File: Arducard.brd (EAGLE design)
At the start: 90 x 50 mm, 19 parts, among them U1 ATMEGA328P, U2 MPR121V2, U3 TPS61097-33DBVR, Y1 8MHZ

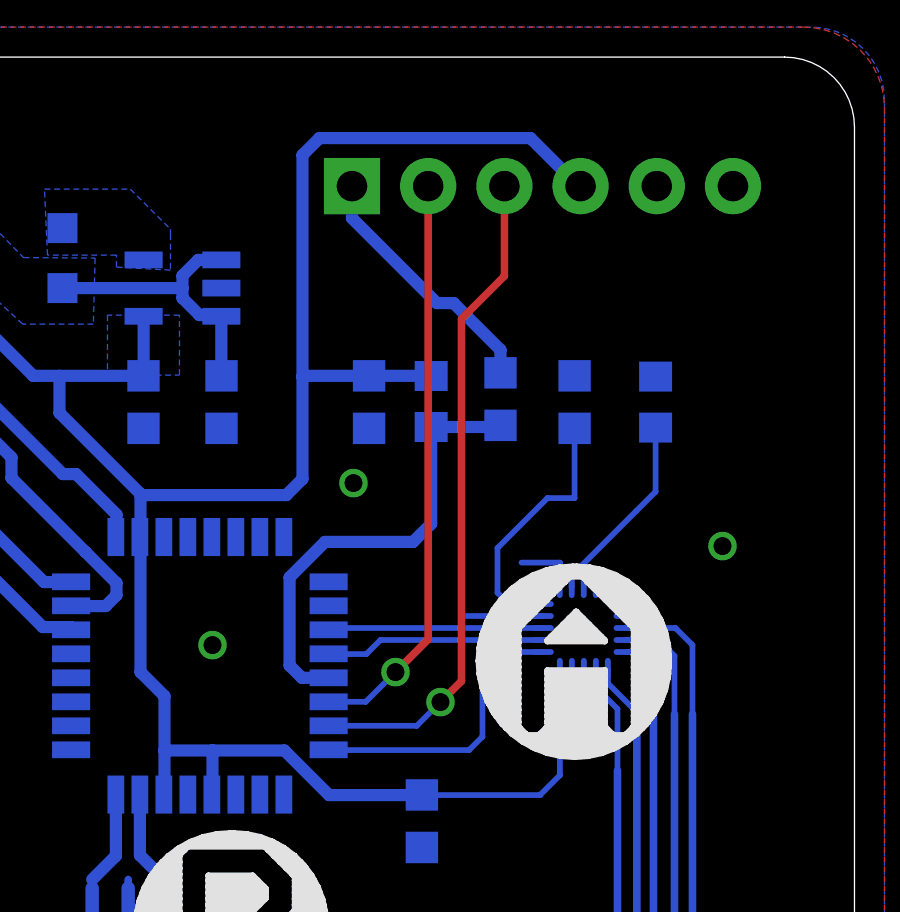
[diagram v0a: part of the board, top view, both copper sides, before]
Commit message: Fixed minor errors
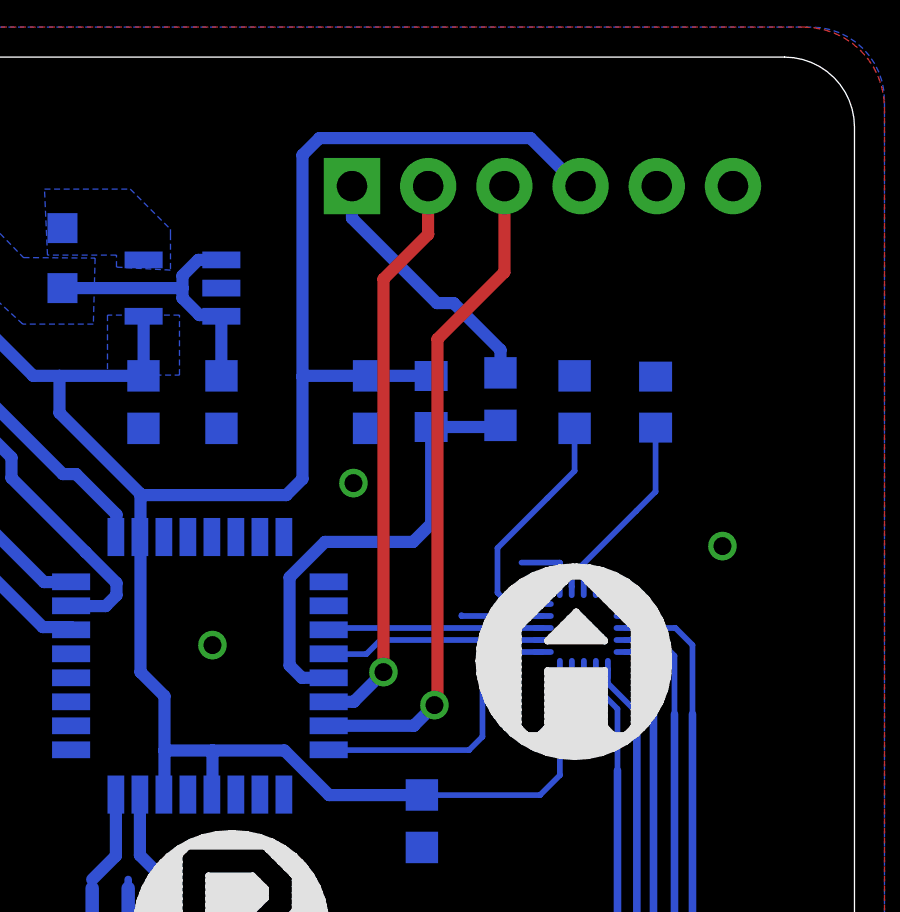
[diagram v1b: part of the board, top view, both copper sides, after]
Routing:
- net N$6: track 8.73 -> 8.20 mm
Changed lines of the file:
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@@
 </class>
 </classes>
-<designrules name="oshPark *">
+<designrules name="oshPark">
 <description language="de">&lt;b&gt;EAGLE Design Rules&lt;/b&gt;
 &lt;p&gt;
@@
 <param name="mlMinCreamFrame" value="0mil"/>
 <param name="mlMaxCreamFrame" value="0mil"/>
-<param name="mlViaStopLimit" value="25mil"/>
+<param name="mlViaStopLimit" value="0mil"/>
 <param name="srRoundness" value="0"/>
 <param name="srMinRoundness" value="0mil"/>
@@
 <wire x1="78.1" y1="32.14801875" x2="78.1" y2="33.63566875" width="0.1905" layer="16"/>
 <wire x1="78.1" y1="33.63566875" x2="79.76433125" y2="35.3" width="0.1905" layer="16"/>
-<wire x1="79.76433125" y1="35.3" x2="80.67" y2="35.3" width="0.1905" layer="16"/>
-<wire x1="80.67" y1="35.3" x2="80.67" y2="37.625" width="0.1905" layer="16"/>
+<wire x1="79.76433125" y1="35.3" x2="80.67" y2="36.20566875" width="0.1905" layer="16"/>
+<wire x1="80.67" y1="36.20566875" x2="80.67" y2="37.625" width="0.1905" layer="16"/>
 </signal>
 <signal name="N$10">
@@
 <contactref element="JP1" pad="P$2"/>
 <contactref element="U1" pad="30"/>
-<wire x1="72.4726" y1="28.51" x2="73.71" y2="28.51" width="0.1905" layer="16"/>
-<wire x1="73.71" y1="28.51" x2="74.7" y2="29.5" width="0.1905" layer="16"/>
-<via x="74.7" y="29.5" extent="1-16" drill="0.6"/>
-<wire x1="74.7" y1="29.5" x2="75.79" y2="30.59" width="0.254" layer="1"/>
-<wire x1="75.79" y1="30.59" x2="75.79" y2="45.7" width="0.254" layer="1"/>
+<wire x1="72.4726" y1="28.51" x2="73.31" y2="28.51" width="0.4064" layer="16"/>
+<wire x1="73.31" y1="28.51" x2="74.3" y2="29.5" width="0.4064" layer="16"/>
+<via x="74.3" y="29.5" extent="1-16" drill="0.6"/>
+<wire x1="74.3" y1="29.5" x2="74.3" y2="42.6" width="0.4064" layer="1"/>
+<wire x1="74.3" y1="42.6" x2="75.79" y2="44.09" width="0.4064" layer="1"/>
+<wire x1="75.79" y1="44.09" x2="75.79" y2="45.7" width="0.4064" layer="1"/>
 </signal>
 <signal name="TX">
 <contactref element="JP1" pad="P$3"/>
 <contactref element="U1" pad="31"/>
-<wire x1="72.4726" y1="27.71" x2="75.41" y2="27.71" width="0.1905" layer="16"/>
-<wire x1="75.41" y1="27.71" x2="76.2" y2="28.5" width="0.1905" layer="16"/>
-<via x="76.2" y="28.5" extent="1-16" drill="0.6"/>
-<wire x1="76.2" y1="28.5" x2="76.9" y2="29.2" width="0.254" layer="1"/>
-<wire x1="76.9" y1="29.2" x2="76.9" y2="41.27" width="0.254" layer="1"/>
-<wire x1="76.9" y1="41.27" x2="78.33" y2="42.7" width="0.254" layer="1"/>
-<wire x1="78.33" y1="42.7" x2="78.33" y2="45.7" width="0.254" layer="1"/>
+<wire x1="72.4726" y1="27.71" x2="75.31" y2="27.71" width="0.4064" layer="16"/>
+<wire x1="75.31" y1="27.71" x2="76" y2="28.4" width="0.4064" layer="16"/>
+<via x="76" y="28.4" extent="1-16" drill="0.6"/>
+<wire x1="76" y1="28.4" x2="76.1" y2="28.4" width="0.4064" layer="1"/>
+<wire x1="76.1" y1="28.4" x2="76.1" y2="40.6" width="0.4064" layer="1"/>
+<wire x1="76.1" y1="40.6" x2="78.33" y2="42.83" width="0.4064" layer="1"/>
+<wire x1="78.33" y1="42.83" x2="78.33" y2="45.7" width="0.4064" layer="1"/>
 </signal>
 </signals>

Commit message: Arducard Board (Eagle)
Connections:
- net RX: now also JP1.P$3; no longer JP1.P$2
- net TX: now also JP1.P$2; no longer JP1.P$3
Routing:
- net TX: track 22.1 -> 19.3 mm
- net RX: track 19.1 -> 17.4 mm
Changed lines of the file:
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@@
 </signal>
 <signal name="RX">
-<contactref element="JP1" pad="P$2"/>
 <contactref element="U1" pad="30"/>
 <wire x1="72.4726" y1="28.51" x2="73.31" y2="28.51" width="0.4064" layer="16"/>
@@
 <wire x1="74.3" y1="29.5" x2="74.3" y2="42.6" width="0.4064" layer="1"/>
 <wire x1="74.3" y1="42.6" x2="75.79" y2="44.09" width="0.4064" layer="1"/>
-<wire x1="75.79" y1="44.09" x2="75.79" y2="45.7" width="0.4064" layer="1"/>
+<contactref element="JP1" pad="P$3"/>
+<wire x1="75.79" y1="44.09" x2="78.33" y2="45.7" width="0" layer="19" extent="1-1"/>
 </signal>
 <signal name="TX">
-<contactref element="JP1" pad="P$3"/>
 <contactref element="U1" pad="31"/>
 <wire x1="72.4726" y1="27.71" x2="75.31" y2="27.71" width="0.4064" layer="16"/>
@@
 <wire x1="76.1" y1="28.4" x2="76.1" y2="40.6" width="0.4064" layer="1"/>
 <wire x1="76.1" y1="40.6" x2="78.33" y2="42.83" width="0.4064" layer="1"/>
-<wire x1="78.33" y1="42.83" x2="78.33" y2="45.7" width="0.4064" layer="1"/>
+<contactref element="JP1" pad="P$2"/>
+<wire x1="78.33" y1="42.83" x2="75.79" y2="45.7" width="0" layer="19" extent="1-1"/>
 </signal>
 </signals>

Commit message: Arducard Board (Eagle)
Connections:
- net RX: now also JP1.P$2; no longer JP1.P$3
- net TX: now also JP1.P$3; no longer JP1.P$2
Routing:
- net TX: track 19.3 -> 22.1 mm
- net RX: track 17.4 -> 19.1 mm
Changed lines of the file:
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@@
 </signal>
 <signal name="RX">
+<contactref element="JP1" pad="P$2"/>
 <contactref element="U1" pad="30"/>
 <wire x1="72.4726" y1="28.51" x2="73.31" y2="28.51" width="0.4064" layer="16"/>
@@
 <wire x1="74.3" y1="29.5" x2="74.3" y2="42.6" width="0.4064" layer="1"/>
 <wire x1="74.3" y1="42.6" x2="75.79" y2="44.09" width="0.4064" layer="1"/>
-<contactref element="JP1" pad="P$3"/>
-<wire x1="75.79" y1="44.09" x2="78.33" y2="45.7" width="0" layer="19" extent="1-1"/>
+<wire x1="75.79" y1="44.09" x2="75.79" y2="45.7" width="0.4064" layer="1"/>
 </signal>
 <signal name="TX">
+<contactref element="JP1" pad="P$3"/>
 <contactref element="U1" pad="31"/>
 <wire x1="72.4726" y1="27.71" x2="75.31" y2="27.71" width="0.4064" layer="16"/>
@@
 <wire x1="76.1" y1="28.4" x2="76.1" y2="40.6" width="0.4064" layer="1"/>
 <wire x1="76.1" y1="40.6" x2="78.33" y2="42.83" width="0.4064" layer="1"/>
-<contactref element="JP1" pad="P$2"/>
-<wire x1="78.33" y1="42.83" x2="75.79" y2="45.7" width="0" layer="19" extent="1-1"/>
+<wire x1="78.33" y1="42.83" x2="78.33" y2="45.7" width="0.4064" layer="1"/>
 </signal>
 </signals>
